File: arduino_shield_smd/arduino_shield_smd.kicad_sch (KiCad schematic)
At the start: 44 parts, among them J1 Power, J2 Digital/PWM, J3 Analog, J4 Digital/PWM, J5 1X5 2.5mm, J6 1x2 2.5mm, U1 PCF8574T, U2 ULN2803A, U3 PCF8574T, U4 ULN2803A

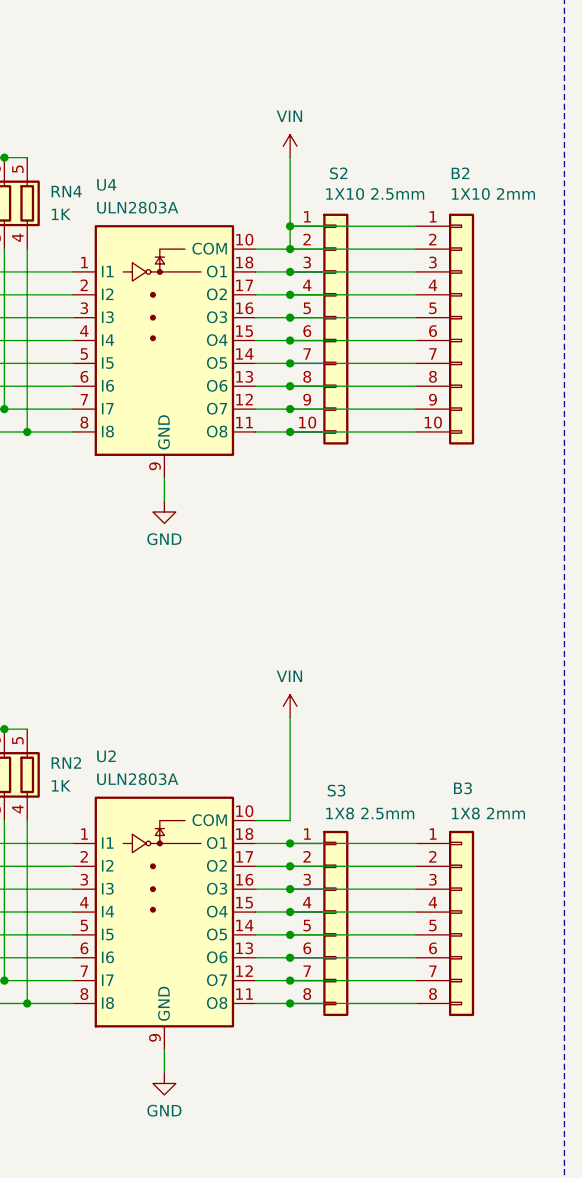
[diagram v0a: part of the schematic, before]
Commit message: Fix pinout for solenoid headers
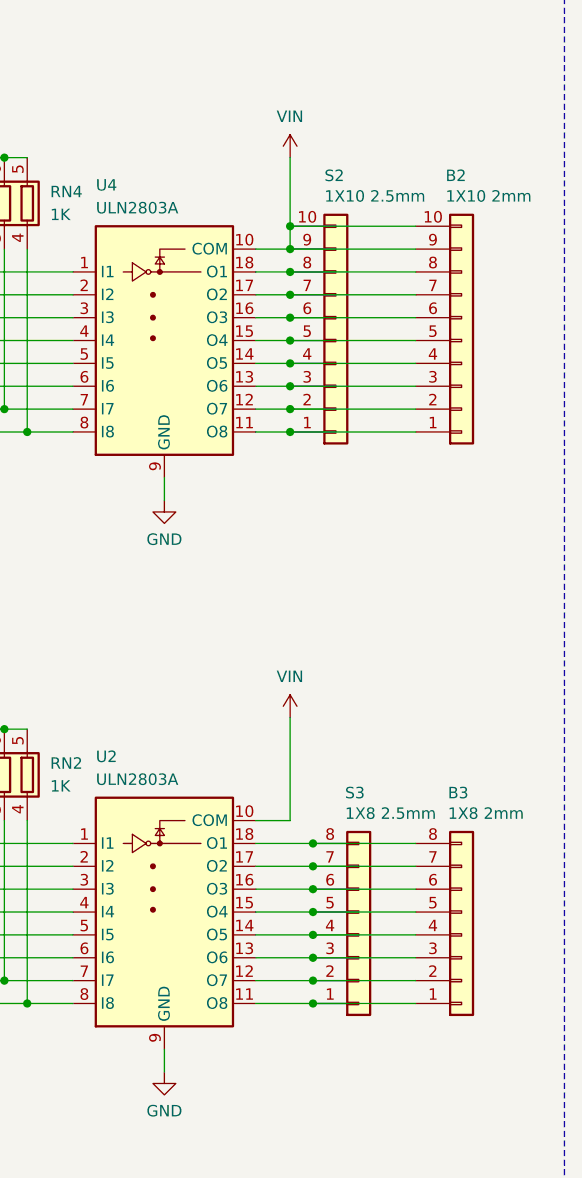
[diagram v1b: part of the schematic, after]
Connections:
- net VIN: now also B2.10 (Pin_10), B2.9 (Pin_9), S2.10 (Pin_10), S2.9 (Pin_9); no longer B2.1 (Pin_1), B2.2 (Pin_2), S2.1 (Pin_1), S2.2 (Pin_2)
- net at B3.1 (Pin_1), S3.1 (Pin_1): now also U2.11 (O8); no longer U2.18 (O1)
- net at B3.2 (Pin_2), S3.2 (Pin_2): now also U2.12 (O7); no longer U2.17 (O2)
- net at B3.3 (Pin_3), S3.3 (Pin_3): now also U2.13 (O6); no longer U2.16 (O3)
- net at B3.4 (Pin_4), S3.4 (Pin_4): now also U2.14 (O5); no longer U2.15 (O4)
- net at B3.5 (Pin_5), S3.5 (Pin_5): now also U2.15 (O4); no longer U2.14 (O5)
- net at B3.6 (Pin_6), S3.6 (Pin_6): now also U2.16 (O3); no longer U2.13 (O6)
- net at B3.7 (Pin_7), S3.7 (Pin_7): now also U2.17 (O2); no longer U2.12 (O7)
- net at B3.8 (Pin_8), S3.8 (Pin_8): now also U2.18 (O1); no longer U2.11 (O8)
- net at B2.3 (Pin_3), S2.3 (Pin_3): now also U4.13 (O6); no longer U4.18 (O1)
- net at B2.4 (Pin_4), S2.4 (Pin_4): now also U4.14 (O5); no longer U4.17 (O2)
- net at B2.5 (Pin_5), S2.5 (Pin_5): now also U4.15 (O4); no longer U4.16 (O3)
- net at B2.6 (Pin_6), S2.6 (Pin_6): now also U4.16 (O3); no longer U4.15 (O4)
- net at B2.7 (Pin_7), S2.7 (Pin_7): now also U4.17 (O2); no longer U4.14 (O5)
- net at B2.8 (Pin_8), S2.8 (Pin_8): now also U4.18 (O1); no longer U4.13 (O6)
- new net: B2.1 (Pin_1), S2.1 (Pin_1), U4.11 (O8)
- new net: B2.2 (Pin_2), S2.2 (Pin_2), U4.12 (O7)
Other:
- moved on the sheet: S3

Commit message: Tweak top silkscreen
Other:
- company: AYAB Project -> Woolly Logic
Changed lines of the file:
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@@
 		(title "AYAB arduino_shield_smd")
 		(date "2025-04-16")
-		(rev "1.5THT")
-		(company "AYAB Project")
+		(rev "KI02.1")
+		(company "Woolly Logic")
 	)
 	(text "ARDUINO"

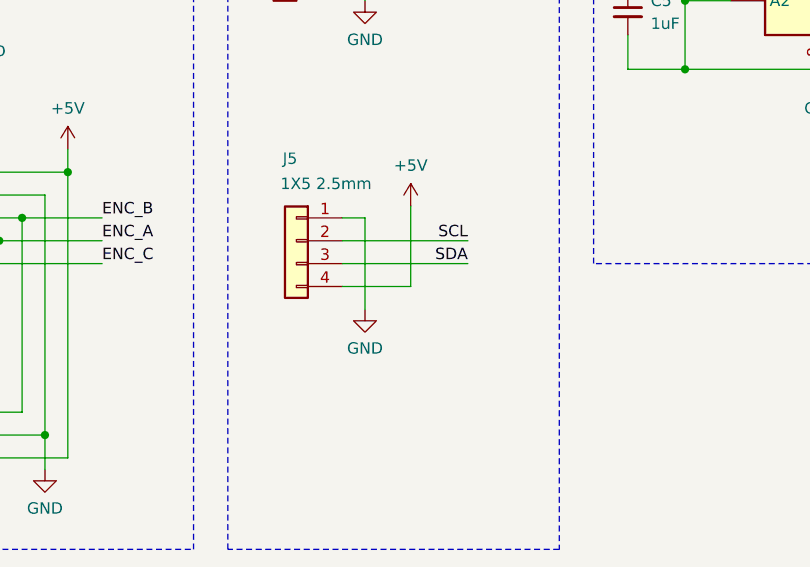
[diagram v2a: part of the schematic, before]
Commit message: Tweak footprints
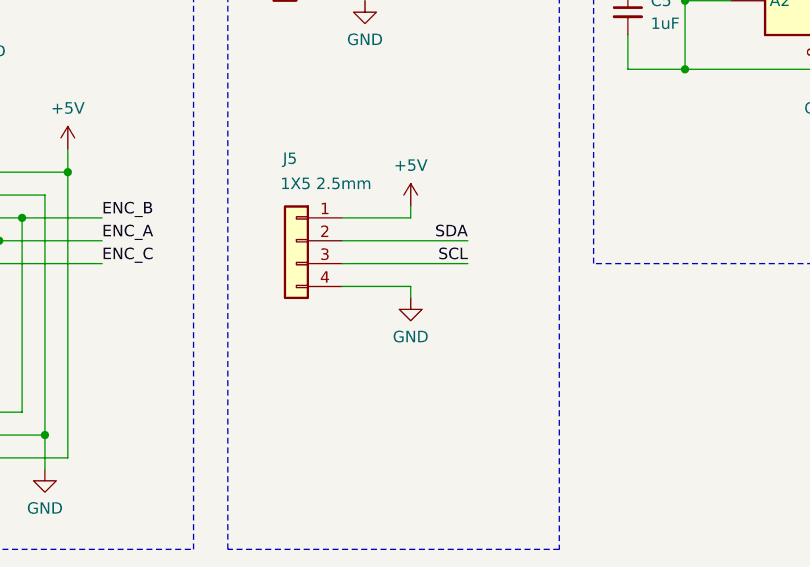
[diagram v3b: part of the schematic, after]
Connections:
- net +5V: now also J5.1 (Pin_1); no longer J5.4 (Pin_4)
- net GND: now also J5.4 (Pin_4); no longer J5.1 (Pin_1)
- net SCL: now also J5.3 (Pin_3); no longer J5.2 (Pin_2)
- net SDA: now also J5.2 (Pin_2); no longer J5.3 (Pin_3)
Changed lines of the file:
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@@
 	(wire
 		(pts
-			(xy 135.89 156.21) (xy 135.89 165.1)
-		)
-		(stroke
-			(width 0)
-			(type default)
-		)
-	)
-	(wire
-		(pts
 			(xy 193.04 62.23) (xy 214.63 62.23)
 		)
@@
 	(wire
 		(pts
-			(xy 128.27 160.02) (xy 142.24 160.02)
+			(xy 251.46 64.77) (xy 265.43 64.77)
 		)
 		(stroke
@@
 	(wire
 		(pts
-			(xy 251.46 64.77) (xy 265.43 64.77)
+			(xy 247.65 130.81) (xy 254 130.81)
 		)
 		(stroke
@@
 	(wire
 		(pts
-			(xy 247.65 130.81) (xy 254 130.81)
+			(xy 161.29 69.85) (xy 161.29 77.47)
 		)
 		(stroke
@@
 	(wire
 		(pts
-			(xy 161.29 69.85) (xy 161.29 77.47)
+			(xy 193.04 54.61) (xy 200.66 54.61)
 		)
 		(stroke
@@
 	(wire
 		(pts
-			(xy 193.04 54.61) (xy 200.66 54.61)
+			(xy 144.78 43.18) (xy 144.78 45.72)
 		)
 		(stroke
@@
 	(wire
 		(pts
-			(xy 144.78 43.18) (xy 144.78 45.72)
+			(xy 128.27 66.04) (xy 144.78 66.04)
 		)
 		(stroke
@@
 	(wire
 		(pts
-			(xy 128.27 66.04) (xy 144.78 66.04)
+			(xy 142.24 160.02) (xy 128.27 160.02)
 		)
 		(stroke
@@
 	(wire
 		(pts
-			(xy 128.27 157.48) (xy 130.81 157.48)
-		)
-		(stroke
-			(width 0)
-			(type default)
-		)
-	)
-	(wire
-		(pts
 			(xy 251.46 46.99) (xy 251.46 49.53)
 		)
@@
 	(wire
 		(pts
+			(xy 135.89 165.1) (xy 135.89 166.37)
+		)
+		(stroke
+			(width 0)
+			(type default)
+		)
+	)
+	(wire
+		(pts
 			(xy 191.77 115.57) (xy 198.12 115.57)
 		)
@@
 	(wire
 		(pts
-			(xy 128.27 162.56) (xy 142.24 162.56)
-		)
-		(stroke
-			(width 0)
-			(type default)
-		)
-	)
-	(wire
-		(pts
 			(xy 62.23 68.58) (xy 82.55 68.58)
 		)
@@
 	(wire
 		(pts
+			(xy 128.27 157.48) (xy 135.89 157.48)
+		)
+		(stroke
+			(width 0)
+			(type default)
+		)
+	)
+	(wire
+		(pts
 			(xy 39.37 66.04) (xy 30.48 66.04)
 		)
@@
 	(wire
 		(pts
+			(xy 135.89 156.21) (xy 135.89 157.48)
+		)
+		(stroke
+			(width 0)
+			(type default)
+		)
+	)
+	(wire
+		(pts
 			(xy 35.56 172.72) (xy 35.56 175.26)
 		)
@@
 	(wire
 		(pts
-			(xy 217.17 39.37) (xy 219.71 39.37)
+			(xy 128.27 165.1) (xy 135.89 165.1)
 		)
 		(stroke
@@
 	(wire
 		(pts
-			(xy 127 118.11) (xy 134.62 118.11)
+			(xy 217.17 39.37) (xy 219.71 39.37)
 		)
 		(stroke
@@
 	(wire
 		(pts
-			(xy 200.66 102.87) (xy 203.2 102.87)
+			(xy 127 118.11) (xy 134.62 118.11)
 		)
 		(stroke
@@
 	(wire
 		(pts
-			(xy 128.27 165.1) (xy 135.89 165.1)
+			(xy 200.66 102.87) (xy 203.2 102.87)
 		)
 		(stroke
@@
 	(wire
 		(pts
-			(xy 130.81 157.48) (xy 130.81 167.64)
-		)
-		(stroke
-			(width 0)
-			(type default)
-		)
-	)
-	(wire
-		(pts
 			(xy 30.48 68.58) (xy 39.37 68.58)
 		)
@@
 	(wire
 		(pts
+			(xy 128.27 162.56) (xy 142.24 162.56)
+		)
+		(stroke
+			(width 0)
+			(type default)
+		)
+	)
+	(wire
+		(pts
 			(xy 161.29 77.47) (xy 182.88 77.47)
 		)
@@
 	)
 	(label "SCL"
-		(at 142.24 160.02 180)
+		(at 142.24 162.56 180)
 		(effects
 			(font
@@
 	)
 	(label "SDA"
-		(at 142.24 162.56 180)
+		(at 142.24 160.02 180)
 		(effects
 			(font
@@
 	(symbol
 		(lib_id "power:GND")
-		(at 130.81 167.64 0)
+		(at 135.89 166.37 0)
 		(mirror y)
 		(unit 1)
@@
 		(dnp no)
 		(property "Reference" "#PWR035"
-			(at 130.81 173.99 0)
+			(at 135.89 172.72 0)
 			(effects
 				(font
@@
 		)
 		(property "Value" "GND"
-			(at 130.81 172.72 0)
+			(at 135.89 171.45 0)
 			(effects
 				(font
@@
 		)
 		(property "Footprint" ""
-			(at 130.81 167.64 0)
+			(at 135.89 166.37 0)
 			(effects
 				(font
@@
 		)
 		(property "Datasheet" ""
-			(at 130.81 167.64 0)
+			(at 135.89 166.37 0)
 			(effects
 				(font
@@
 		)
 		(property "Description" "Power symbol creates a global label with name \"GND\" , ground"
-			(at 130.81 167.64 0)
+			(at 135.89 166.37 0)
 			(effects
 				(font
